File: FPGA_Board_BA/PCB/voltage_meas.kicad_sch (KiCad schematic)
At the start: 4 parts, among them U101 HV_Probe, U1501 HV_Probe, U1502 HV_Probe, U1503 HV_Probe

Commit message: work
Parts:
- renumbered U1501 to U18, U1502 to U19, U1503 to U20, U101 to U21
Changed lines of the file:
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@@
 		(on_board yes)
 		(dnp no)
-		(property "Reference" "U101"
+		(property "Reference" "U21"
 			(at 125.095 36.83 0)
 			(effects
@@
 			(project "FPGA_Board_BA"
 				(path "/fd7503bc-e7fc-4766-b224-3d1c3d7de5ff/bf010b8c-6832-4a61-9247-eaeb93645cb7"
-					(reference "U101")
+					(reference "U21")
 					(unit 1)
 				)
@@
 		(dnp no)
 		(fields_autoplaced yes)
-		(property "Reference" "#PWR01505"
+		(property "Reference" "#PWR0104"
 			(at 100.33 96.52 0)
 			(effects
@@
 			(project "FPGA_Board_BA"
 				(path "/fd7503bc-e7fc-4766-b224-3d1c3d7de5ff/bf010b8c-6832-4a61-9247-eaeb93645cb7"
-					(reference "#PWR01505")
+					(reference "#PWR0104")
 					(unit 1)
 				)
@@
 		(dnp no)
 		(fields_autoplaced yes)
-		(property "Reference" "#PWR01503"
+		(property "Reference" "#PWR0106"
 			(at 100.33 130.81 0)
 			(effects
@@
 			(project ""
 				(path "/fd7503bc-e7fc-4766-b224-3d1c3d7de5ff/bf010b8c-6832-4a61-9247-eaeb93645cb7"
-					(reference "#PWR01503")
+					(reference "#PWR0106")
 					(unit 1)
 				)
@@
 		(dnp no)
 		(fields_autoplaced yes)
-		(property "Reference" "#PWR01507"
+		(property "Reference" "#PWR0101"
 			(at 99.06 45.72 0)
 			(effects
@@
 			(project ""
 				(path "/fd7503bc-e7fc-4766-b224-3d1c3d7de5ff/bf010b8c-6832-4a61-9247-eaeb93645cb7"
-					(reference "#PWR01507")
+					(reference "#PWR0101")
 					(unit 1)
 				)
@@
 		(dnp no)
 		(fields_autoplaced yes)
-		(property "Reference" "#PWR01508"
+		(property "Reference" "#PWR0103"
 			(at 100.33 81.28 0)
 			(effects
@@
 			(project "FPGA_Board_BA"
 				(path "/fd7503bc-e7fc-4766-b224-3d1c3d7de5ff/bf010b8c-6832-4a61-9247-eaeb93645cb7"
-					(reference "#PWR01508")
+					(reference "#PWR0103")
 					(unit 1)
 				)
@@
 		(on_board yes)
 		(dnp no)
-		(property "Reference" "U1503"
+		(property "Reference" "U20"
 			(at 123.825 138.43 0)
 			(effects
@@
 			(project "FPGA_Board_BA"
 				(path "/fd7503bc-e7fc-4766-b224-3d1c3d7de5ff/bf010b8c-6832-4a61-9247-eaeb93645cb7"
-					(reference "U1503")
+					(reference "U20")
 					(unit 1)
 				)
@@
 		(on_board yes)
 		(dnp no)
-		(property "Reference" "U1502"
+		(property "Reference" "U19"
 			(at 123.825 106.68 0)
 			(effects
@@
 			(project "FPGA_Board_BA"
 				(path "/fd7503bc-e7fc-4766-b224-3d1c3d7de5ff/bf010b8c-6832-4a61-9247-eaeb93645cb7"
-					(reference "U1502")
+					(reference "U19")
 					(unit 1)
 				)
@@
 		(dnp no)
 		(fields_autoplaced yes)
-		(property "Reference" "#PWR01504"
+		(property "Reference" "#PWR0108"
 			(at 101.6 163.83 0)
 			(effects
@@
 			(project "FPGA_Board_BA"
 				(path "/fd7503bc-e7fc-4766-b224-3d1c3d7de5ff/bf010b8c-6832-4a61-9247-eaeb93645cb7"
-					(reference "#PWR01504")
+					(reference "#PWR0108")
 					(unit 1)
 				)
@@
 		(dnp no)
 		(fields_autoplaced yes)
-		(property "Reference" "#PWR01506"
+		(property "Reference" "#PWR0102"
 			(at 99.06 62.23 0)
 			(effects
@@
 			(project "FPGA_Board_BA"
 				(path "/fd7503bc-e7fc-4766-b224-3d1c3d7de5ff/bf010b8c-6832-4a61-9247-eaeb93645cb7"
-					(reference "#PWR01506")
+					(reference "#PWR0102")
 					(unit 1)
 				)
@@
 		(dnp no)
 		(fields_autoplaced yes)
-		(property "Reference" "#PWR01510"
+		(property "Reference" "#PWR0107"
 			(at 101.6 147.32 0)
 			(effects
@@
 			(project "FPGA_Board_BA"
 				(path "/fd7503bc-e7fc-4766-b224-3d1c3d7de5ff/bf010b8c-6832-4a61-9247-eaeb93645cb7"
-					(reference "#PWR01510")
+					(reference "#PWR0107")
 					(unit 1)
 				)
@@
 		(dnp no)
 		(fields_autoplaced yes)
-		(property "Reference" "#PWR01509"
+		(property "Reference" "#PWR0105"
 			(at 100.33 115.57 0)
 			(effects
@@
 			(project "FPGA_Board_BA"
 				(path "/fd7503bc-e7fc-4766-b224-3d1c3d7de5ff/bf010b8c-6832-4a61-9247-eaeb93645cb7"
-					(reference "#PWR01509")
+					(reference "#PWR0105")
 					(unit 1)
 				)
@@
 		(on_board yes)
 		(dnp no)
-		(property "Reference" "U1501"
+		(property "Reference" "U18"
 			(at 123.825 72.39 0)
 			(effects
@@
 			(project "FPGA_Board_BA"
 				(path "/fd7503bc-e7fc-4766-b224-3d1c3d7de5ff/bf010b8c-6832-4a61-9247-eaeb93645cb7"
-					(reference "U1501")
-					(unit 1)
-				)
+					(reference "U18")
+					(unit 1)
+				)

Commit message: 22.11
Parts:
- renumbered U18 to U12, U19 to U13, U20 to U14, U21 to U15
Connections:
- net +5V renamed +5VA
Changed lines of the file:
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@@
 		(on_board yes)
 		(dnp no)
-		(property "Reference" "U21"
+		(property "Reference" "U15"
 			(at 125.095 36.83 0)
 			(effects
@@
 			(project "FPGA_Board_BA"
 				(path "/fd7503bc-e7fc-4766-b224-3d1c3d7de5ff/bf010b8c-6832-4a61-9247-eaeb93645cb7"
-					(reference "U21")
+					(reference "U15")
 					(unit 1)
 				)
@@
 		(dnp no)
 		(fields_autoplaced yes)
-		(property "Reference" "#PWR0104"
+		(property "Reference" "#PWR097"
 			(at 100.33 96.52 0)
 			(effects
@@
 			(project "FPGA_Board_BA"
 				(path "/fd7503bc-e7fc-4766-b224-3d1c3d7de5ff/bf010b8c-6832-4a61-9247-eaeb93645cb7"
-					(reference "#PWR0104")
+					(reference "#PWR097")
 					(unit 1)
 				)
@@
 		(dnp no)
 		(fields_autoplaced yes)
-		(property "Reference" "#PWR0106"
+		(property "Reference" "#PWR099"
 			(at 100.33 130.81 0)
 			(effects
@@
 			(project ""
 				(path "/fd7503bc-e7fc-4766-b224-3d1c3d7de5ff/bf010b8c-6832-4a61-9247-eaeb93645cb7"
-					(reference "#PWR0106")
-					(unit 1)
-				)
-			)
-		)
-	)
-	(symbol
-		(lib_id "power:+5V")
+					(reference "#PWR099")
+					(unit 1)
+				)
+			)
+		)
+	)
+	(symbol
+		(lib_id "power:+5VA")
 		(at 99.06 41.91 0)
 		(unit 1)
@@
 		(dnp no)
 		(fields_autoplaced yes)
-		(property "Reference" "#PWR0101"
+		(property "Reference" "#PWR094"
 			(at 99.06 45.72 0)
 			(effects
@@
 			)
 		)
-		(property "Value" "+5V"
+		(property "Value" "+5VA"
 			(at 99.06 36.83 0)
 			(effects
@@
 			)
 		)
-		(property "Description" "Power symbol creates a global label with name \"+5V\""
+		(property "Description" "Power symbol creates a global label with name \"+5VA\""
 			(at 99.06 41.91 0)
 			(effects
@@
 		)
 		(instances
-			(project ""
-				(path "/fd7503bc-e7fc-4766-b224-3d1c3d7de5ff/bf010b8c-6832-4a61-9247-eaeb93645cb7"
-					(reference "#PWR0101")
-					(unit 1)
-				)
-			)
-		)
-	)
-	(symbol
-		(lib_id "power:+5V")
-		(at 100.33 77.47 0)
-		(unit 1)
-		(exclude_from_sim no)
-		(in_bom yes)
-		(on_board yes)
-		(dnp no)
-		(fields_autoplaced yes)
-		(property "Reference" "#PWR0103"
-			(at 100.33 81.28 0)
-			(effects
-				(font
-					(size 1.27 1.27)
-				)
-				(hide yes)
-			)
-		)
-		(property "Value" "+5V"
-			(at 100.33 72.39 0)
-			(effects
-				(font
-					(size 1.27 1.27)
-				)
-			)
-		)
-		(property "Footprint" ""
-			(at 100.33 77.47 0)
-			(effects
-				(font
-					(size 1.27 1.27)
-				)
-				(hide yes)
-			)
-		)
-		(property "Datasheet" ""
-			(at 100.33 77.47 0)
-			(effects
-				(font
-					(size 1.27 1.27)
-				)
-				(hide yes)
-			)
-		)
-		(property "Description" "Power symbol creates a global label with name \"+5V\""
-			(at 100.33 77.47 0)
-			(effects
-				(font
-					(size 1.27 1.27)
-				)
-				(hide yes)
-			)
-		)
-		(pin "1"
-		)
-		(instances
-			(project "FPGA_Board_BA"
-				(path "/fd7503bc-e7fc-4766-b224-3d1c3d7de5ff/bf010b8c-6832-4a61-9247-eaeb93645cb7"
-					(reference "#PWR0103")
+			(project "FPGA_Board_BA"
+				(path "/fd7503bc-e7fc-4766-b224-3d1c3d7de5ff/bf010b8c-6832-4a61-9247-eaeb93645cb7"
+					(reference "#PWR094")
 					(unit 1)
 				)
@@
 		(on_board yes)
 		(dnp no)
-		(property "Reference" "U20"
+		(property "Reference" "U14"
 			(at 123.825 138.43 0)
 			(effects
@@
 			(project "FPGA_Board_BA"
 				(path "/fd7503bc-e7fc-4766-b224-3d1c3d7de5ff/bf010b8c-6832-4a61-9247-eaeb93645cb7"
-					(reference "U20")
+					(reference "U14")
 					(unit 1)
 				)
@@
 		(on_board yes)
 		(dnp no)
-		(property "Reference" "U19"
+		(property "Reference" "U13"
 			(at 123.825 106.68 0)
 			(effects
@@
 			(project "FPGA_Board_BA"
 				(path "/fd7503bc-e7fc-4766-b224-3d1c3d7de5ff/bf010b8c-6832-4a61-9247-eaeb93645cb7"
-					(reference "U19")
+					(reference "U13")
 					(unit 1)
 				)
@@
 		(dnp no)
 		(fields_autoplaced yes)
-		(property "Reference" "#PWR0108"
+		(property "Reference" "#PWR0101"
 			(at 101.6 163.83 0)
 			(effects
@@
 			(project "FPGA_Board_BA"
 				(path "/fd7503bc-e7fc-4766-b224-3d1c3d7de5ff/bf010b8c-6832-4a61-9247-eaeb93645cb7"
-					(reference "#PWR0108")
+					(reference "#PWR0101")
+					(unit 1)
+				)
+			)
+		)
+	)
+	(symbol
+		(lib_id "power:+5VA")
+		(at 101.6 143.51 0)
+		(unit 1)
+		(exclude_from_sim no)
+		(in_bom yes)
+		(on_board yes)
+		(dnp no)
+		(fields_autoplaced yes)
+		(property "Reference" "#PWR0100"
+			(at 101.6 147.32 0)
+			(effects
+				(font
+					(size 1.27 1.27)
+				)
+				(hide yes)
+			)
+		)
+		(property "Value" "+5VA"
+			(at 101.6 138.43 0)
+			(effects
+				(font
+					(size 1.27 1.27)
+				)
+			)
+		)
+		(property "Footprint" ""
+			(at 101.6 143.51 0)
+			(effects
+				(font
+					(size 1.27 1.27)
+				)
+				(hide yes)
+			)
+		)
+		(property "Datasheet" ""
+			(at 101.6 143.51 0)
+			(effects
+				(font
+					(size 1.27 1.27)
+				)
+				(hide yes)
+			)
+		)
+		(property "Description" "Power symbol creates a global label with name \"+5VA\""
+			(at 101.6 143.51 0)
+			(effects
+				(font
+					(size 1.27 1.27)
+				)
+				(hide yes)
+			)
+		)
+		(pin "1"
+		)
+		(instances
+			(project "FPGA_Board_BA"
+				(path "/fd7503bc-e7fc-4766-b224-3d1c3d7de5ff/bf010b8c-6832-4a61-9247-eaeb93645cb7"
+					(reference "#PWR0100")
 					(unit 1)
 				)
@@
 		(dnp no)
 		(fields_autoplaced yes)
-		(property "Reference" "#PWR0102"
+		(property "Reference" "#PWR095"
 			(at 99.06 62.23 0)
 			(effects
@@
 			(project "FPGA_Board_BA"
 				(path "/fd7503bc-e7fc-4766-b224-3d1c3d7de5ff/bf010b8c-6832-4a61-9247-eaeb93645cb7"
-					(reference "#PWR0102")
-					(unit 1)
-				)
-			)
-		)
-	)
-	(symbol
-		(lib_id "power:+5V")
-		(at 101.6 143.51 0)
+					(reference "#PWR095")
+					(unit 1)
+				)
+			)
+		)
+	)
+	(symbol
+		(lib_id "power:+5VA")
+		(at 100.33 111.76 0)
 		(unit 1)
 		(exclude_from_sim no)
@@
 		(dnp no)
 		(fields_autoplaced yes)
-		(property "Reference" "#PWR0107"
-			(at 101.6 147.32 0)
-			(effects
-				(font
-					(size 1.27 1.27)
-				)
-				(hide yes)
-			)
-		)
-		(property "Value" "+5V"
-			(at 101.6 138.43 0)
-			(effects
-				(font
-					(size 1.27 1.27)
-				)
-			)
-		)
-		(property "Footprint" ""
-			(at 101.6 143.51 0)
-			(effects
-				(font
-					(size 1.27 1.27)
-				)
-				(hide yes)
-			)
-		)
-		(property "Datasheet" ""
-			(at 101.6 143.51 0)
-			(effects
-				(font
-					(size 1.27 1.27)
-				)
-				(hide yes)
-			)
-		)
-		(property "Description" "Power symbol creates a global label with name \"+5V\""
-			(at 101.6 143.51 0)
-			(effects
-				(font
-					(size 1.27 1.27)
-				)
-				(hide yes)
-			)
-		)
-		(pin "1"
-		)
-		(instances
-			(project "FPGA_Board_BA"
-				(path "/fd7503bc-e7fc-4766-b224-3d1c3d7de5ff/bf010b8c-6832-4a61-9247-eaeb93645cb7"
-					(reference "#PWR0107")
-					(unit 1)
-				)
-			)
-		)
-	)
-	(symbol
-		(lib_id "power:+5V")
-		(at 100.33 111.76 0)
-		(unit 1)
-		(exclude_from_sim no)
-		(in_bom yes)
-		(on_board yes)
-		(dnp no)
-		(fields_autoplaced yes)
-		(property "Reference" "#PWR0105"
+		(property "Reference" "#PWR098"
 			(at 100.33 115.57 0)
 			(effects
@@
 			)
 		)
-		(property "Value" "+5V"
+		(property "Value" "+5VA"
 			(at 100.33 106.68 0)
 			(effects
@@
 			)
 		)
-		(property "Description" "Power symbol creates a global label with name \"+5V\""
+		(property "Description" "Power symbol creates a global label with name \"+5VA\""
 			(at 100.33 111.76 0)
 			(effects
@@
 			(project "FPGA_Board_BA"
 				(path "/fd7503bc-e7fc-4766-b224-3d1c3d7de5ff/bf010b8c-6832-4a61-9247-eaeb93645cb7"
-					(reference "#PWR0105")
+					(reference "#PWR098")
 					(unit 1)
 				)
@@
 		(on_board yes)
 		(dnp no)
-		(property "Reference" "U18"
+		(property "Reference" "U12"
 			(at 123.825 72.39 0)
 			(effects
@@
 			(project "FPGA_Board_BA"
 				(path "/fd7503bc-e7fc-4766-b224-3d1c3d7de5ff/bf010b8c-6832-4a61-9247-eaeb93645cb7"
-					(reference "U18")
-					(unit 1)
-				)
+					(reference "U12")
+					(unit 1)
+				)
+			)
+		)
+	)
+	(symbol
+		(lib_id "power:+5VA")
+		(at 100.33 77.47 0)
+		(unit 1)
+		(exclude_from_sim no)
+		(in_bom yes)
+		(on_board yes)
+		(dnp no)
+		(fields_autoplaced yes)
+		(property "Reference" "#PWR096"
+			(at 100.33 81.28 0)
+			(effects
+				(font
+					(size 1.27 1.27)
+				)
+				(hide yes)
+			)
+		)
+		(property "Value" "+5VA"
+			(at 100.33 72.39 0)
+			(effects
+				(font
+					(size 1.27 1.27)
+				)
+			)
+		)
+		(property "Footprint" ""
+			(at 100.33 77.47 0)
+			(effects
+				(font
+					(size 1.27 1.27)
+				)
+				(hide yes)
+			)
+		)
+		(property "Datasheet" ""
+			(at 100.33 77.47 0)
+			(effects
+				(font
+					(size 1.27 1.27)
+				)
+				(hide yes)
+			)
+		)
+		(property "Description" "Power symbol creates a global label with name \"+5VA\""
+			(at 100.33 77.47 0)
+			(effects
+				(font
+					(size 1.27 1.27)
+				)
+				(hide yes)
+			)
+		)
+		(pin "1"
+		)
+		(instances
+			(project ""
+				(path "/fd7503bc-e7fc-4766-b224-3d1c3d7de5ff/bf010b8c-6832-4a61-9247-eaeb93645cb7"
+					(reference "#PWR096")
+					(unit 1)
+				)

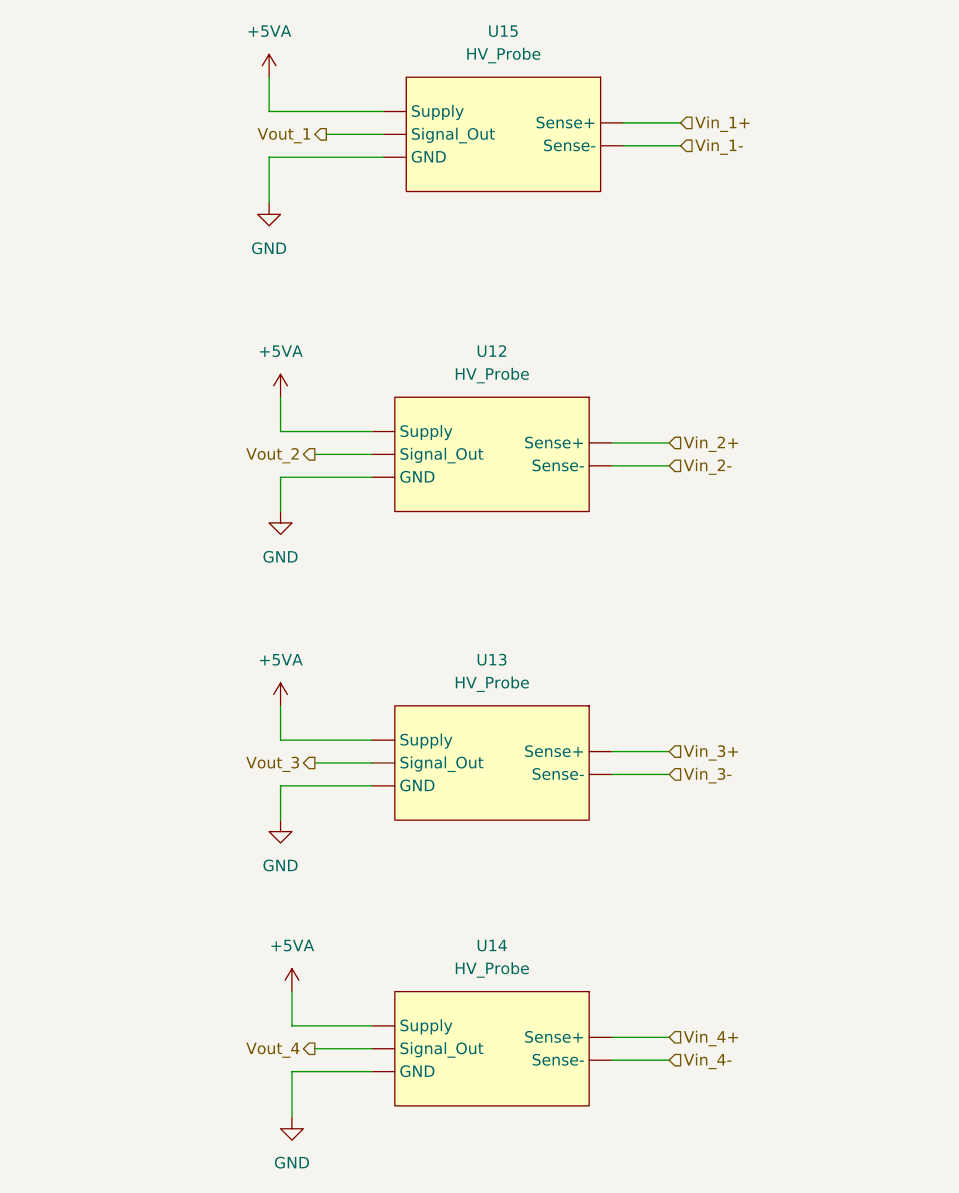
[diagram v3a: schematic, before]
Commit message: component placement with new concept is ready
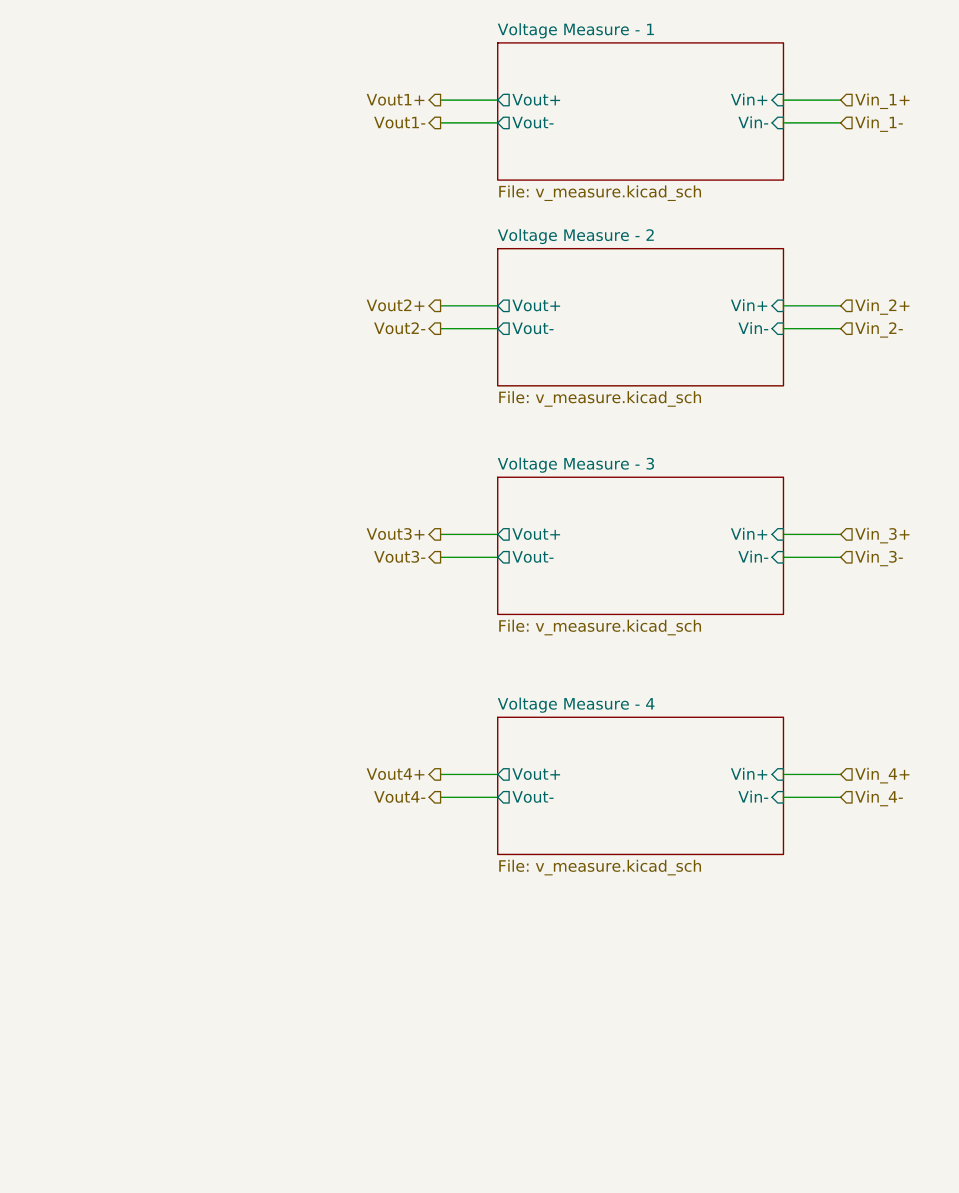
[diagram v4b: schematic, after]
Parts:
- removed U12, U13, U14, U15: HV_Probe, MYLIB_Misc:HV_Probe, symbol MYLIB_Misc:HV_Probe
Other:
- added sheet Voltage Measure - 1 (v_measure.kicad_sch)
- added sheet Voltage Measure - 2 (v_measure.kicad_sch)
- added sheet Voltage Measure - 3 (v_measure.kicad_sch)
- added sheet Voltage Measure - 4 (v_measure.kicad_sch)

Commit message: big schematic cleanup. Added wire to bus
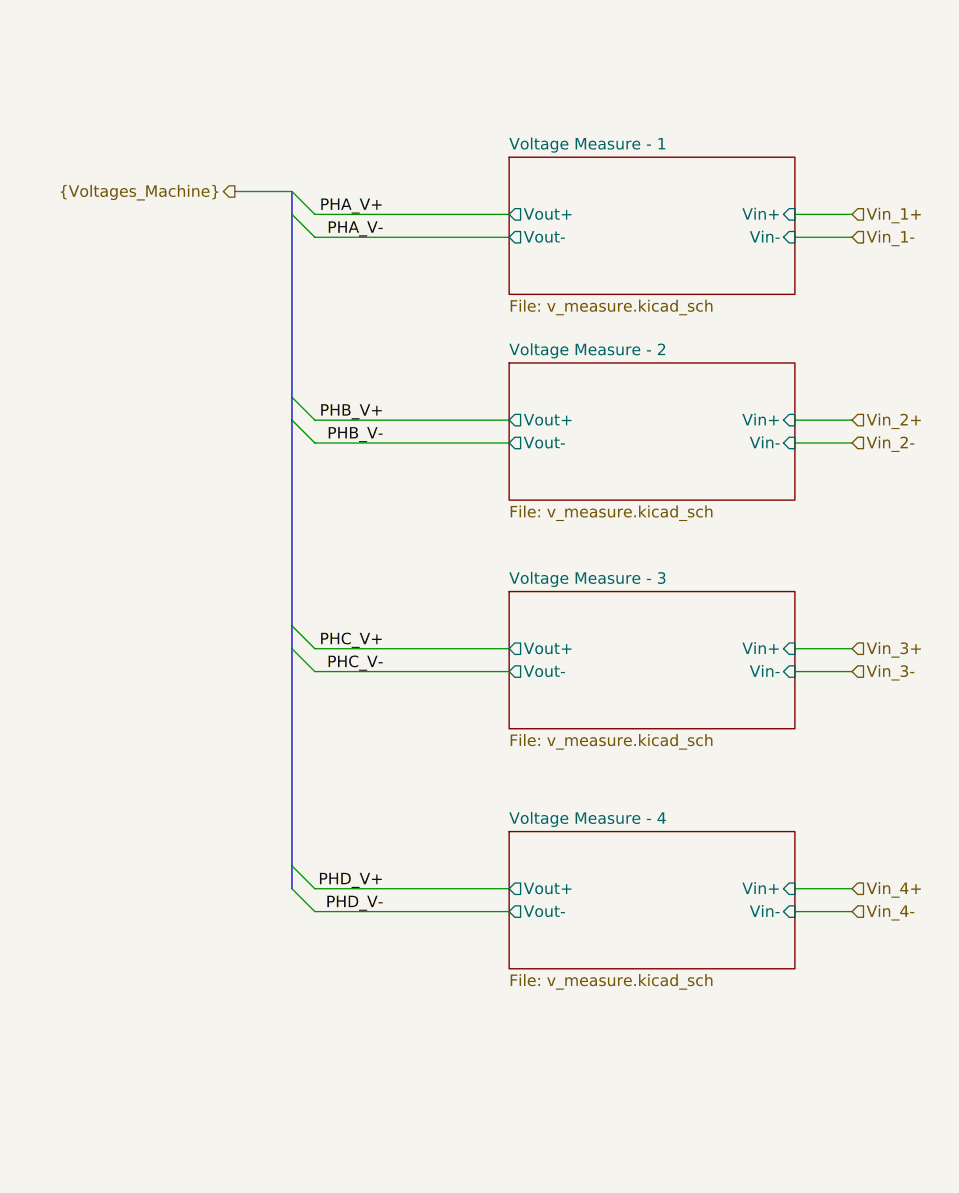
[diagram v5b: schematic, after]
